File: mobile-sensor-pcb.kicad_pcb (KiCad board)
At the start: 2 copper layers, 101.6 x 53.3 mm, 93 parts, among them J1 SMA, J2 USB_OTG, J3 JST PH, Q1 PNP-BJT-BIASED_SOT, SW1 RESET, SW2 ON/OFF, U1 3M_2908-05WB-MG, U10 LP2980AIM5-3.3/NOPB, U11 LP2980AIM5-3.3/NOPB, U12 LP2980AIM5-3.3/NOPB, U13 TPS61030RSA, U2 74HC4050, U3 FGPMMOPA6H, U4 RT9193, U5 MIC5219, U6 MCP73831T-2ACI/OT, U7 MAX31855KASA, U8 MAX31855KASA, U9 MAX31855KASA, X1 XBEE

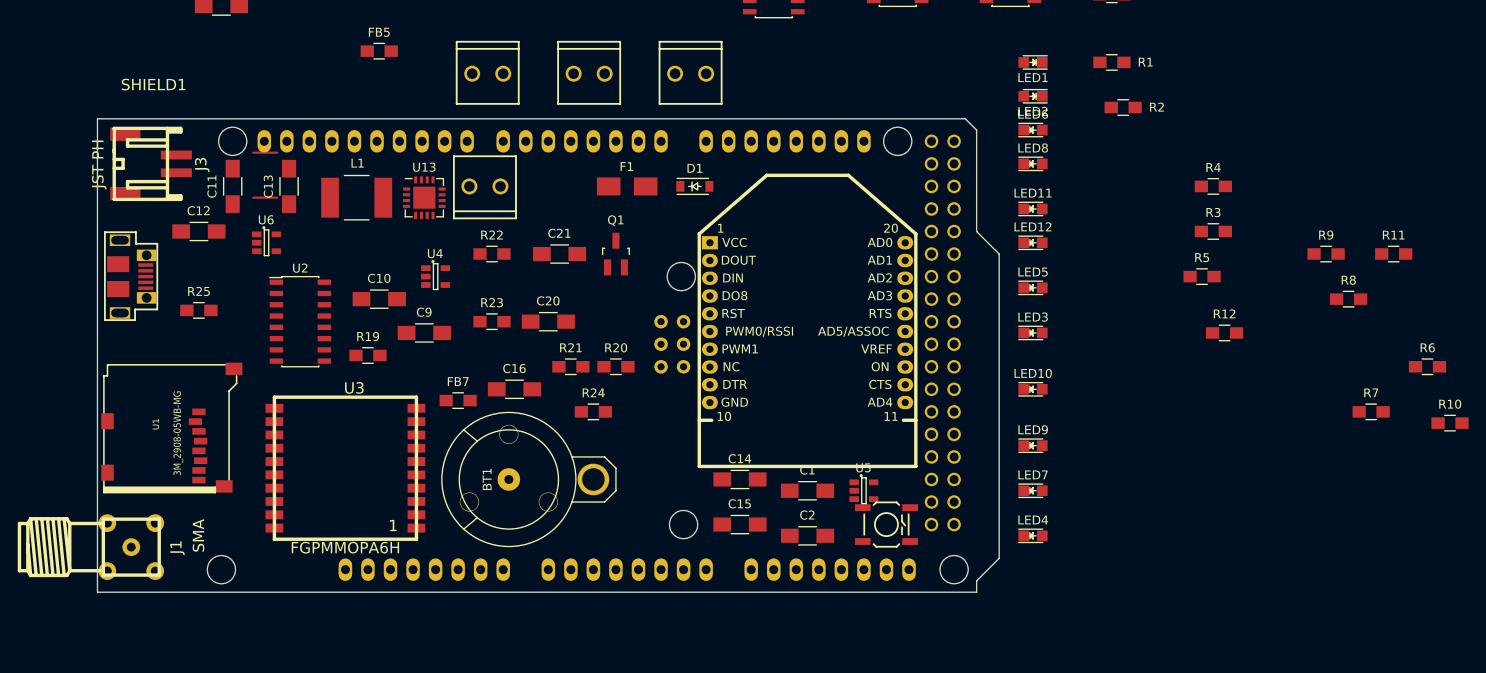
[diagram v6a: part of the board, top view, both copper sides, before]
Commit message: Fix a few bad connections, start to lay out PCB
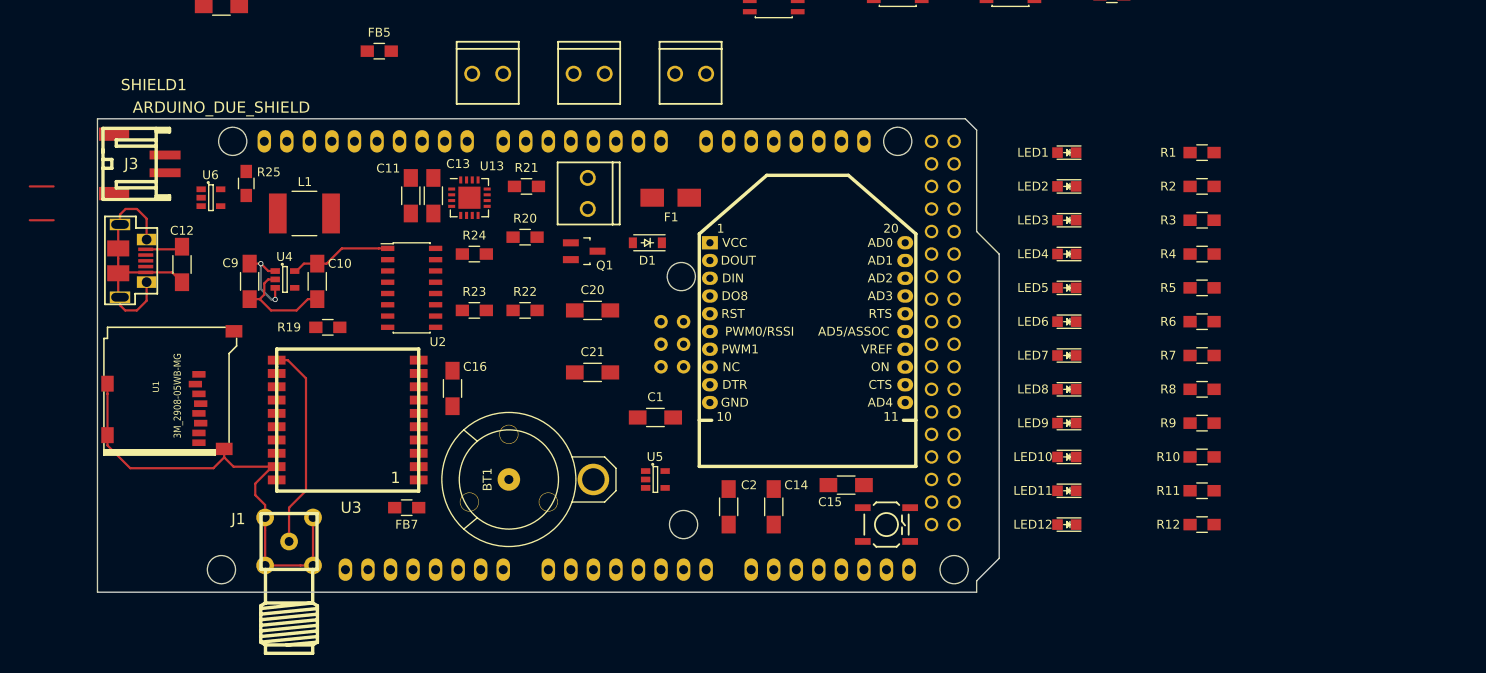
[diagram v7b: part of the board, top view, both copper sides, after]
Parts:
- C1, C10, C11, C12, C2, C3, C4, C5, C6, C7, C8, C9: value 10 uF -> 10uF
- C14, C15, C16: value 100 nF -> 100nF
- C17, C18, C19: value 10 nF -> 10nF
- C20: value 100 uF -> 100uF
- C21: value 2.2 uF -> 2.2uF
- moved R11 34.3 mm to (175.3, 141.0)
- moved LED4 32.0 mm to (160.0, 114.3), turned to 180 degrees
- moved LED11 32.0 mm to (160.0, 141.0), turned to 180 degrees
- moved LED12 32.0 mm to (160.0, 144.8), turned to 180 degrees
- moved R10 28.2 mm to (175.3, 137.2)
- moved R6 25.9 mm to (175.3, 121.9)
- moved LED8 25.7 mm to (160.0, 129.5), turned to 180 degrees
- moved R9 23.6 mm to (175.3, 133.3)
- moved U5 23.5 mm to (113.7, 139.7)
- moved R24 22.3 mm to (93.3, 114.3)
- moved LED6 21.9 mm to (160.0, 121.9), turned to 180 degrees
- moved R12 21.7 mm to (175.3, 144.8)
- moved R21 20.9 mm to (99.1, 106.7)
- moved C9 20.5 mm to (67.9, 117.4), turned to 270 degrees
- moved C11 20.1 mm to (86.1, 107.7), turned to 270 degrees
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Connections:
- C14 pad 1: Net-(C14-Pad1) -> XBEE-3V3
- FB7 pad 2: Net-(FB7-Pad2) -> Net-(C16-Pad1)
- J1 pad 3: Net-(J1-Pad3) -> GND
- J1 pad 4: Net-(J1-Pad4) -> GND
- J2 pad 6: Net-(J2-Pad6) -> GND
- U13 pad 12: Net-(U13-Pad12) -> Net-(Q1-Pad1)
- U13 pad 15: Net-(U13-Pad15) -> Net-(C20-Pad1)
- U13 pad 6: Net-(U13-Pad6) -> GND
- U13 pad 7: Net-(U13-Pad7) -> GND
- U3 pad 1: Net-(FB7-Pad2) -> Net-(C16-Pad1)
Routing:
- net GND: track 0.00 -> 94.6 mm
- net Net-(J1-Pad1): track 0.00 -> 23.3 mm
- net GPS-SD-3V3: track 0.00 -> 11.5 mm
- net BATT-5V: track 0.00 -> 9.49 mm, vias 0 -> 2
- net USB-5V: track 0.00 -> 4.20 mm
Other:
- net class Default: trace_width 0.25 -> 0.254; via_dia 0.6 -> 0.5842
- rule trace_min: 0.2 -> 0.1778

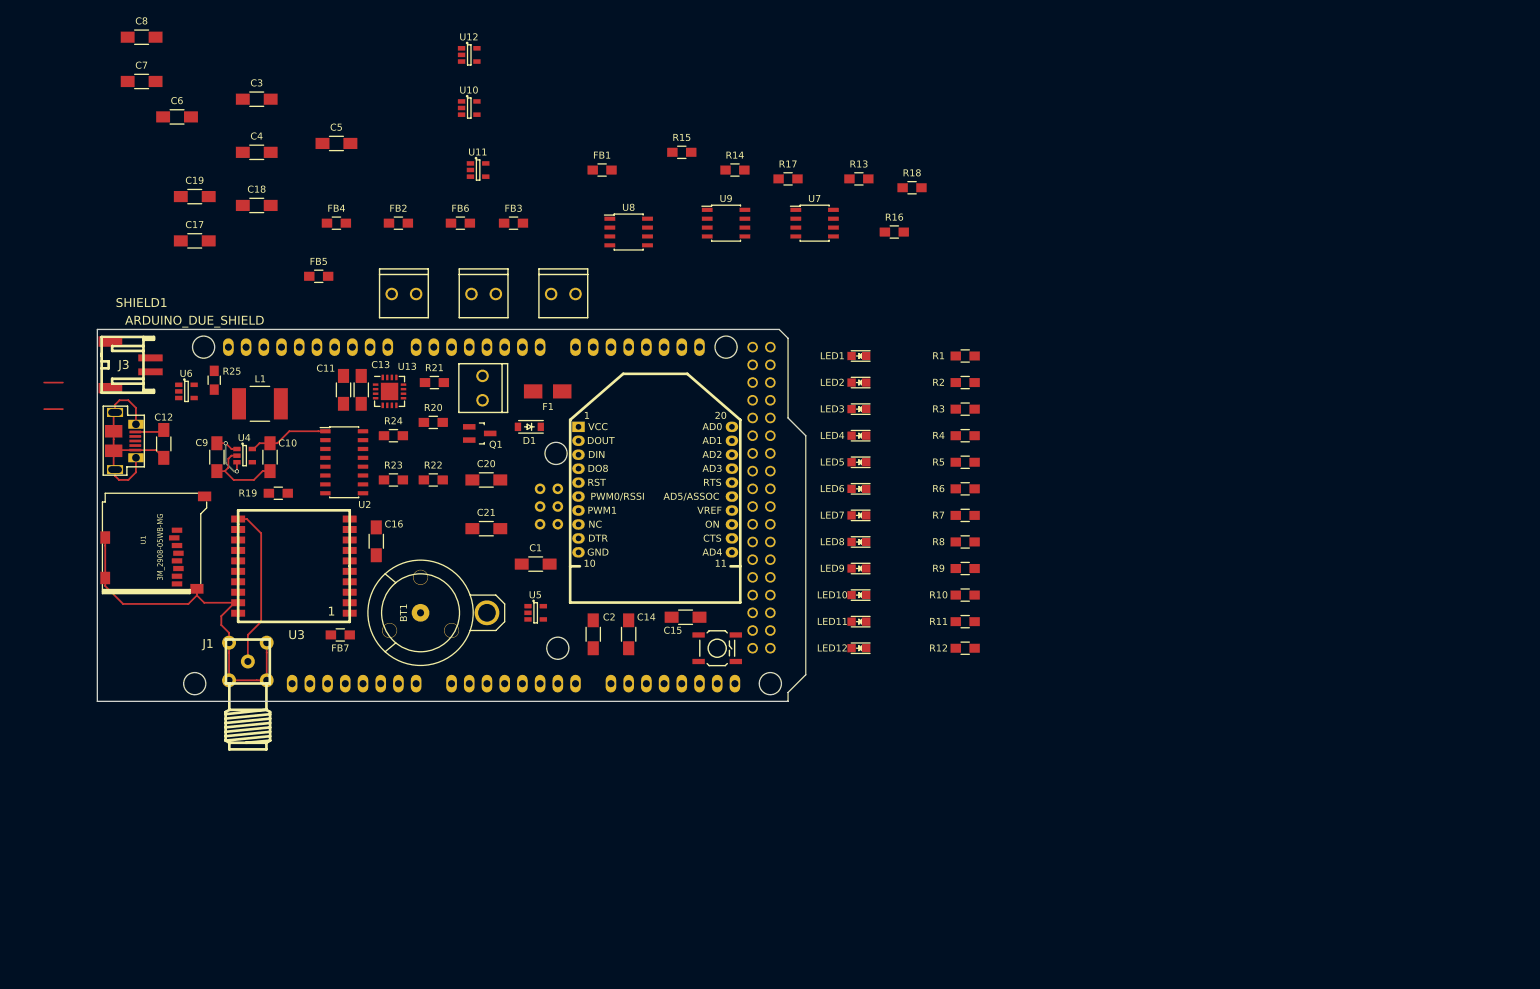
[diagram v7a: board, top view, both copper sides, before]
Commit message: Arrange thermocouple amps
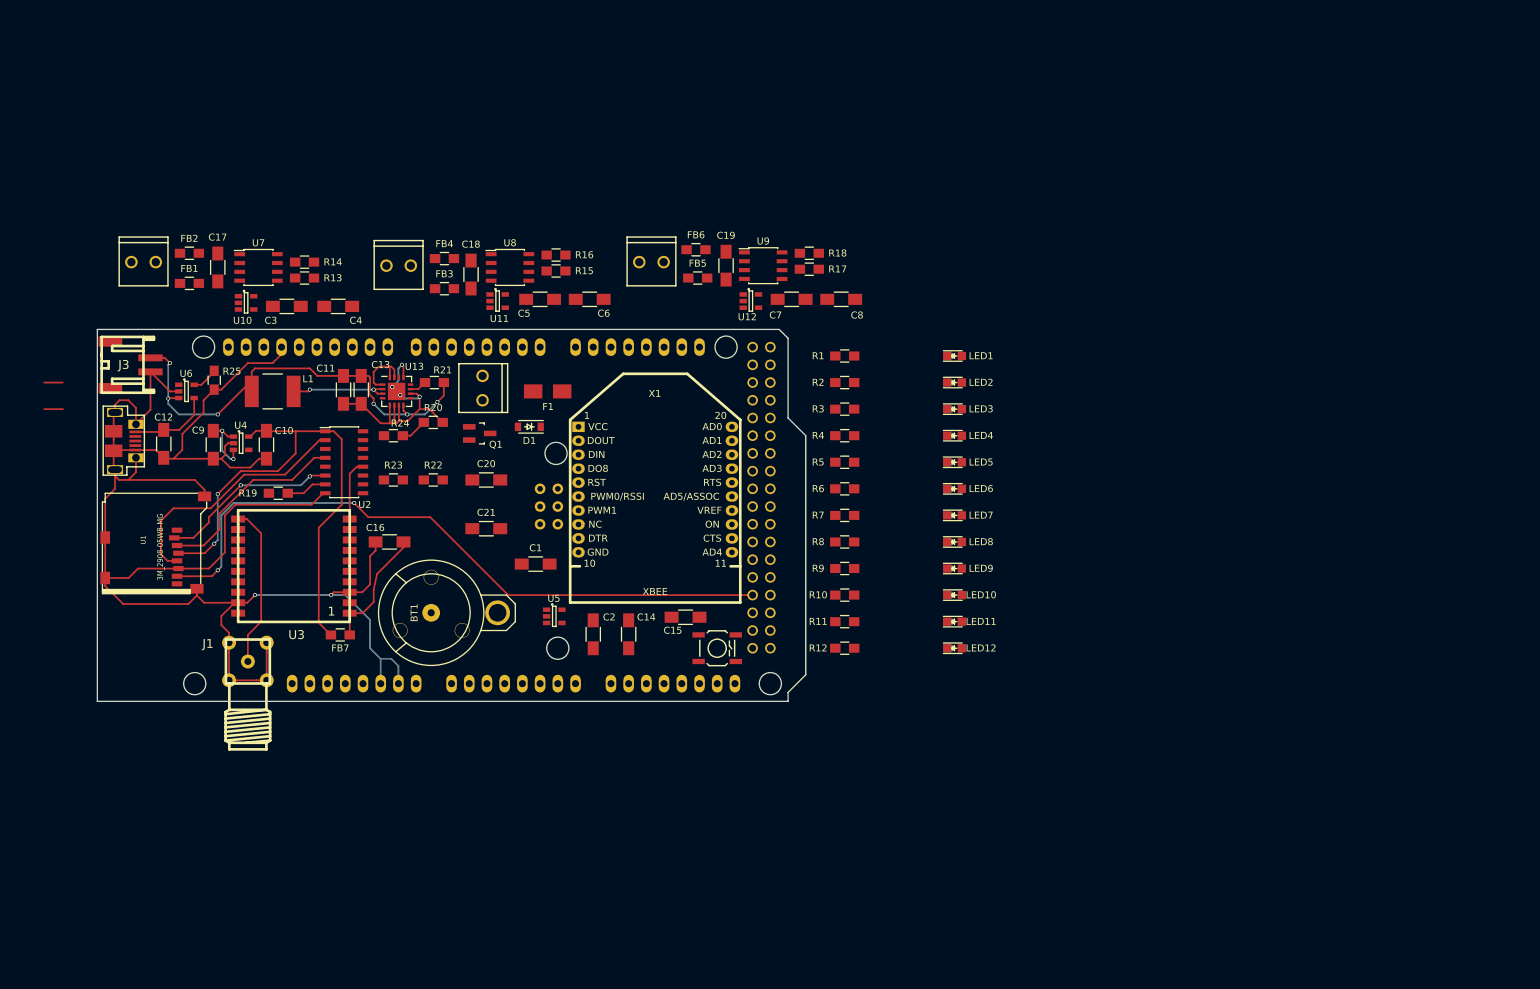
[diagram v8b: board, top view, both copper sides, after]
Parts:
- moved C8 107.1 mm to (157.5, 94.7), turned to 180 degrees
- moved C7 98.3 mm to (150.4, 94.7)
- moved R13 80.8 mm to (80.5, 91.7), turned to 180 degrees
- moved U7 80.0 mm to (73.9, 90.2)
- moved C19 76.8 mm to (141.0, 89.9), turned to 90 degrees
- moved C6 64.7 mm to (121.4, 94.7), turned to 180 degrees
- moved R14 63.1 mm to (80.5, 89.4), turned to 180 degrees
- moved FB1 61.4 mm to (64.0, 92.5)
- moved TC1 60.4 mm to (59.2, 89.4)
- moved FB5 54.4 mm to (136.9, 91.7)
- moved U12 53.6 mm to (144.5, 95.0)
- moved R16 48.6 mm to (116.6, 88.4), turned to 180 degrees
- moved U10 42.5 mm to (72.1, 95.2)
- moved C5 36.8 mm to (114.3, 94.7)
- moved FB6 34.0 mm to (136.7, 87.6)
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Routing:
- net GND: track 94.6 -> 295.3 mm, vias 0 -> 6
- net SD-MISO: track 0.00 -> 96.7 mm, vias 0 -> 2
- net Net-(C11-Pad1): track 0.00 -> 65.0 mm, vias 0 -> 6
- net GPS-SD-3V3: track 11.5 -> 74.1 mm, vias 0 -> 2
- net Net-(U1-Pad5): track 0.00 -> 35.8 mm
- net Net-(U1-Pad3): track 0.00 -> 27.8 mm
- net Net-(U1-Pad2): track 0.00 -> 25.8 mm, vias 0 -> 2
- net Net-(C16-Pad1): track 0.00 -> 17.5 mm
- net Net-(L1-Pad2): track 0.00 -> 14.5 mm, vias 0 -> 2
- net Net-(C20-Pad1): track 0.00 -> 9.14 mm
- net GPS-3V3-RX: track 0.00 -> 8.82 mm
- net USB-5V: track 4.20 -> 11.9 mm
- net SD-CS: track 0.00 -> 5.92 mm
- net Net-(R20-Pad1): track 0.00 -> 3.80 mm
- net Net-(R25-Pad1): track 0.00 -> 3.80 mm
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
